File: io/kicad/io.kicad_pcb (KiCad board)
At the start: 2 copper layers, 90 x 88.4 mm, 52 parts, among them J1 Conn_01x04_Pin, J2 Conn_01x04_Pin, J3 pcie_98, U1 B0505MT-1WR4, U2 ESD5344D-TP, U3 ESD5344D-TP, U4 ADUM1201ARZ-RL7, U5 ADUM1201ARZ-RL7, U6 XC6206P332MR, U7 XC6206P332MR, U8 ESD5344D-TP

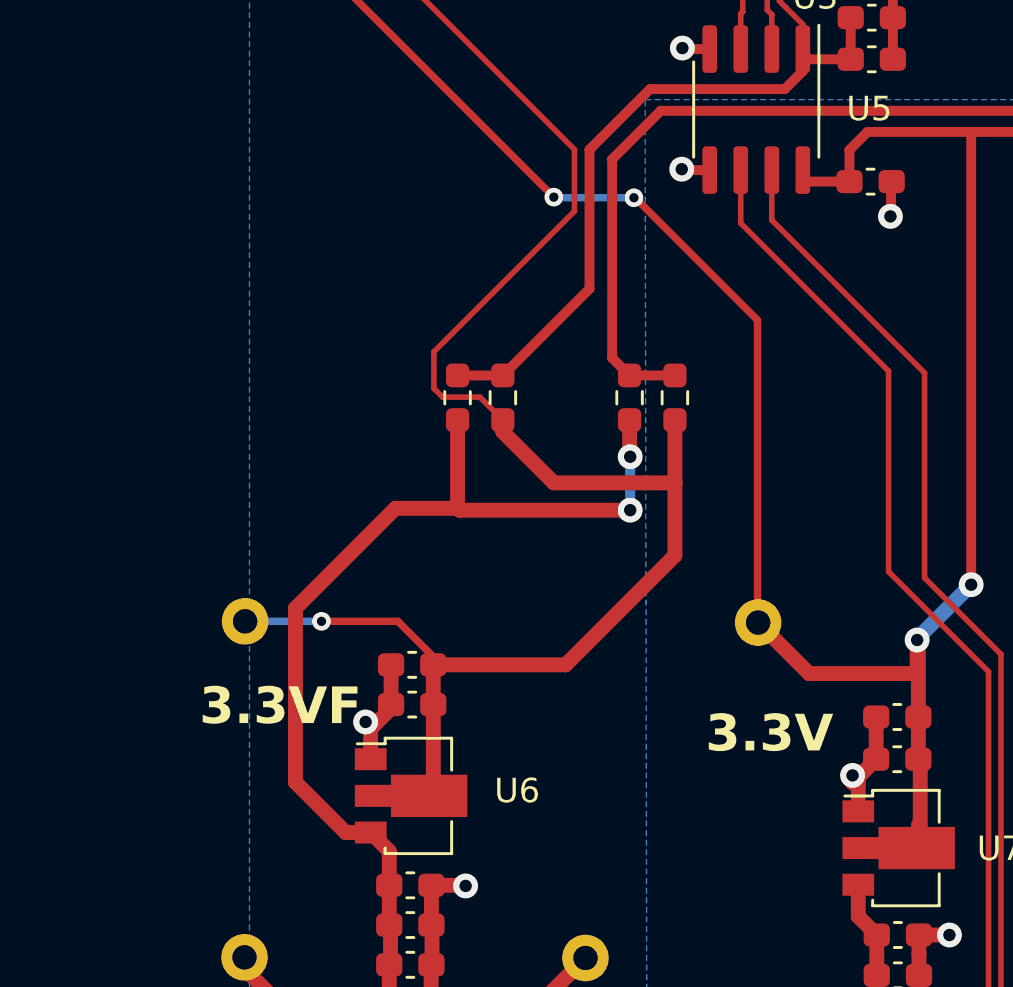
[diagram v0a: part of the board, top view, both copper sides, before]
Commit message: Tweaked the IO card layout
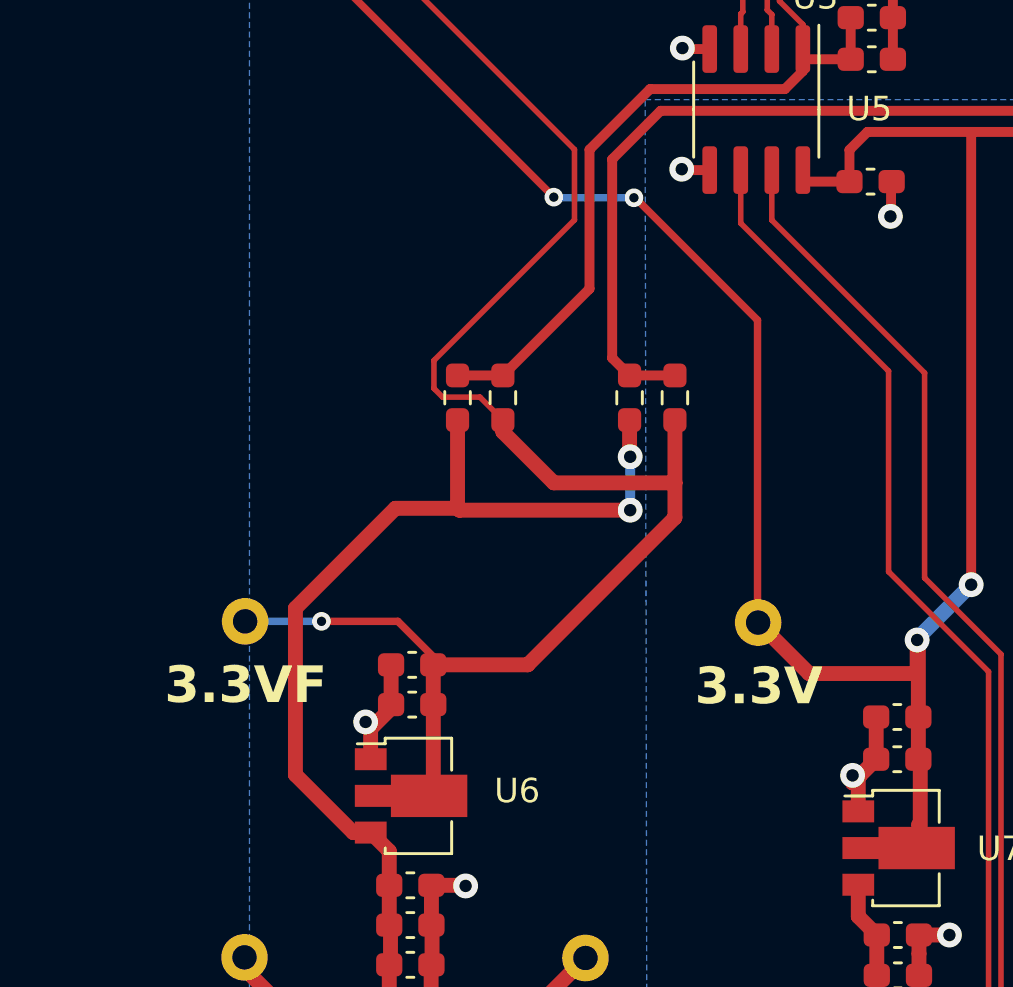
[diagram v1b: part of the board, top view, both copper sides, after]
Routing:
- net /+3V3F: track 71.6 -> 70.7 mm
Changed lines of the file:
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@@
     (effects (font (size 1.5 1.5) (thickness 0.3) bold) (justify bottom mirror))
   )
-  (gr_text "3.3V" (at 8.001 -38.227) (layer "B.SilkS")
-    (effects (font (size 1.5 1.5) (thickness 0.3) bold) (justify left bottom mirror))
+  (gr_text "3.3V" (at 5.2578 -40.259) (layer "B.SilkS")
+    (effects (font (size 1.5 1.5) (thickness 0.3) bold) (justify bottom mirror))
   )
-  (gr_text "3.3VF" (at -14.3002 -39.37) (layer "B.SilkS")
+  (gr_text "3.3VF" (at -15.7226 -40.2336) (layer "B.SilkS")
     (effects (font (size 1.5 1.5) (thickness 0.3) bold) (justify bottom mirror))
   )
@@
     (effects (font (size 1.5 1.5) (thickness 0.3) bold) (justify bottom))
   )
-  (gr_text "3.3V" (at 3.0988 -38.3032) (layer "F.SilkS")
-    (effects (font (size 1.5 1.5) (thickness 0.3) bold) (justify left bottom))
+  (gr_text "3.3V" (at 5.2832 -40.2336) (layer "F.SilkS")
+    (effects (font (size 1.5 1.5) (thickness 0.3) bold) (justify bottom))
   )
   (gr_text "3.3V" (at -18.9484 -83.2104) (layer "F.SilkS")
@@
     (effects (font (size 1.5 1.5) (thickness 0.3) bold) (justify left bottom))
   )
-  (gr_text "3.3VF" (at -14.2748 -39.4208) (layer "F.SilkS")
+  (gr_text "3.3VF" (at -15.6972 -40.2844) (layer "F.SilkS")
     (effects (font (size 1.5 1.5) (thickness 0.3) bold) (justify bottom))
   )
@@
   (via (at -11.8364 -86.614) (size 0.762) (drill 0.381) (layers "F.Cu" "B.Cu") (net 2))
   (via (at 26.9494 -71.7296) (size 0.508) (drill 0.254) (layers "F.Cu" "B.Cu") (net 2))
+  (segment (start -13.6652 -44.2976) (end -9.5758 -48.387) (width 0.6096) (layer "F.Cu") (net 3))
   (segment (start -7.0358 -48.387) (end -6.9596 -48.3108) (width 0.6096) (layer "F.Cu") (net 3))
-  (segment (start -11.6064 -35.1268) (end -13.6652 -37.1856) (width 0.6096) (layer "F.Cu") (net 3))
   (segment (start -7.0358 -51.9957) (end -7.0358 -48.387) (width 0.6096) (layer "F.Cu") (net 3))
   (segment (start -9.8287 -28.4745) (end -9.8287 -29.718) (width 0.6096) (layer "F.Cu") (net 3))
-  (segment (start -10.586 -35.1268) (end -11.6064 -35.1268) (width 0.6096) (layer "F.Cu") (net 3))
+  (segment (start -10.586 -35.1268) (end -11.3016 -35.1268) (width 0.6096) (layer "F.Cu") (net 3))
   (segment (start 0.0254 -50.5714) (end 0.0254 -50.4952) (width 0.6096) (layer "F.Cu") (net 3))
   (segment (start -9.8287 -31.3436) (end -9.8287 -32.9692) (width 0.6096) (layer "F.Cu") (net 3))
@@
   (segment (start -6.9596 -48.3108) (end 0.0254 -48.3108) (width 0.6096) (layer "F.Cu") (net 3))
   (segment (start -11.567 -27.2542) (end -11.049 -27.2542) (width 0.6096) (layer "F.Cu") (net 3))
+  (segment (start -11.3016 -35.1268) (end -13.6652 -37.4904) (width 0.6096) (layer "F.Cu") (net 3))
   (segment (start -15.748 -29.5538) (end -15.748 -30.0228) (width 0.6096) (layer "F.Cu") (net 3))
-  (segment (start -13.6652 -37.1856) (end -13.6652 -44.2976) (width 0.6096) (layer "F.Cu") (net 3))
+  (segment (start -13.6652 -37.4904) (end -13.6652 -44.2976) (width 0.6096) (layer "F.Cu") (net 3))
   (segment (start -9.8287 -34.3695) (end -10.586 -35.1268) (width 0.6096) (layer "F.Cu") (net 3))
   (segment (start -11.567 -27.2542) (end -13.4484 -27.2542) (width 0.6096) (layer "F.Cu") (net 3))
-  (segment (start -13.6652 -44.2976) (end -9.5758 -48.387) (width 0.6096) (layer "F.Cu") (net 3))
+  (segment (start -9.5758 -48.387) (end -7.0358 -48.387) (width 0.6096) (layer "F.Cu") (net 3))
   (segment (start 0.1016 -50.4952) (end 0.0254 -50.5714) (width 0.6096) (layer "F.Cu") (net 3))
   (segment (start 0.0254 -50.4952) (end 0.1016 -50.4952) (width 0.6096) (layer "F.Cu") (net 3))
-  (segment (start -9.5758 -48.387) (end -7.0358 -48.387) (width 0.6096) (layer "F.Cu") (net 3))
   (via (at 0.0254 -50.4952) (size 1.016) (drill 0.508) (layers "F.Cu" "B.Cu") (net 3))
   (via (at 0.0254 -48.3108) (size 1.016) (drill 0.508) (layers "F.Cu" "B.Cu") (net 3))
   (segment (start 0.0254 -50.4952) (end 0.0254 -48.3108) (width 0.4064) (layer "B.Cu") (net 3))
   (segment (start 1.8542 -51.9957) (end 1.8542 -49.4538) (width 0.6096) (layer "F.Cu") (net 4))
-  (segment (start -8.001 -54.7878) (end -2.25301 -60.53579) (width 0.2286) (layer "F.Cu") (net 4))
-  (segment (start 1.8542 -49.403) (end 1.8288 -49.4284) (width 0.6096) (layer "F.Cu") (net 4))
+  (segment (start -5.1816 -51.9957) (end -6.1195 -52.9336) (width 0.2286) (layer "F.Cu") (net 4))
+  (segment (start 1.8542 -48.006) (end 1.8542 -49.403) (width 0.6096) (layer "F.Cu") (net 4))
   (segment (start -9.4742 -43.7642) (end -12.5984 -43.7642) (width 0.3048) (layer "F.Cu") (net 4))
-  (segment (start -5.1816 -51.9957) (end -6.1195 -52.9336) (width 0.2286) (layer "F.Cu") (net 4))
+  (segment (start -8.001 -53.2892) (end -8.001 -54.4322) (width 0.2286) (layer "F.Cu") (net 4))
+  (segment (start -7.6454 -52.9336) (end -8.001 -53.2892) (width 0.2286) (layer "F.Cu") (net 4))
   (segment (start -5.1816 -51.5112) (end -5.1816 -51.9957) (width 0.6096) (layer "F.Cu") (net 4))
   (segment (start 1.8288 -49.4284) (end -3.0988 -49.4284) (width 0.6096) (layer "F.Cu") (net 4))
-  (segment (start -8.001 -53.2892) (end -8.001 -54.7878) (width 0.2286) (layer "F.Cu") (net 4))
+  (segment (start -8.001 -54.4322) (end -2.25301 -60.18019) (width 0.2286) (layer "F.Cu") (net 4))
   (segment (start -8.0286 -42.3186) (end -9.4742 -43.7642) (width 0.3048) (layer "F.Cu") (net 4))
-  (segment (start 1.8542 -46.4566) (end 1.8542 -49.403) (width 0.6096) (layer "F.Cu") (net 4))
-  (segment (start -2.25301 -63.06061) (end -9.3726 -70.1802) (width 0.2286) (layer "F.Cu") (net 4))
-  (segment (start -8.0286 -41.9862) (end -2.6162 -41.9862) (width 0.6096) (layer "F.Cu") (net 4))
   (segment (start -8.0275 -40.2082) (end -8.0264 -40.2071) (width 0.6096) (layer "F.Cu") (net 4))
+  (segment (start -2.25301 -60.18019) (end -2.25301 -63.06061) (width 0.2286) (layer "F.Cu") (net 4))
   (segment (start -9.3726 -70.1802) (end -9.3726 -76.8115) (width 0.2286) (layer "F.Cu") (net 4))
-  (segment (start -7.6454 -52.9336) (end -8.001 -53.2892) (width 0.2286) (layer "F.Cu") (net 4))
+  (segment (start -4.1656 -41.9862) (end 1.8542 -48.006) (width 0.6096) (layer "F.Cu") (net 4))
   (segment (start -6.1195 -52.9336) (end -7.6454 -52.9336) (width 0.2286) (layer "F.Cu") (net 4))
   (segment (start -8.0264 -40.2071) (end -8.0264 -36.72895) (width 0.6096) (layer "F.Cu") (net 4))
+  (segment (start -8.0286 -41.9862) (end -4.1656 -41.9862) (width 0.6096) (layer "F.Cu") (net 4))
   (segment (start -8.0286 -41.8846) (end -8.0286 -40.2093) (width 0.6096) (layer "F.Cu") (net 4))
+  (segment (start -2.25301 -63.06061) (end -9.3726 -70.1802) (width 0.2286) (layer "F.Cu") (net 4))
+  (segment (start 1.8542 -49.403) (end 1.8288 -49.4284) (width 0.6096) (layer "F.Cu") (net 4))
   (segment (start -8.0286 -41.9862) (end -8.0286 -42.3186) (width 0.3048) (layer "F.Cu") (net 4))
-  (segment (start -2.25301 -60.53579) (end -2.25301 -63.06061) (width 0.2286) (layer "F.Cu") (net 4))
   (segment (start -3.0988 -49.4284) (end -5.1816 -51.5112) (width 0.6096) (layer "F.Cu") (net 4))
   (segment (start 1.8542 -49.4538) (end 1.8288 -49.4284) (width 0.6096) (layer "F.Cu") (net 4))
   (segment (start -8.0286 -40.2093) (end -8.0275 -40.2082) (width 0.6096) (layer "F.Cu") (net 4))
-  (segment (start -2.6162 -41.9862) (end 1.8542 -46.4566) (width 0.6096) (layer "F.Cu") (net 4))
   (via (at -12.5984 -43.7642) (size 0.762) (drill 0.381) (layers "F.Cu" "B.Cu") (net 4))
   (segment (start -15.6972 -43.7642) (end -12.5984 -43.7642) (width 0.3048) (layer "B.Cu") (net 4))

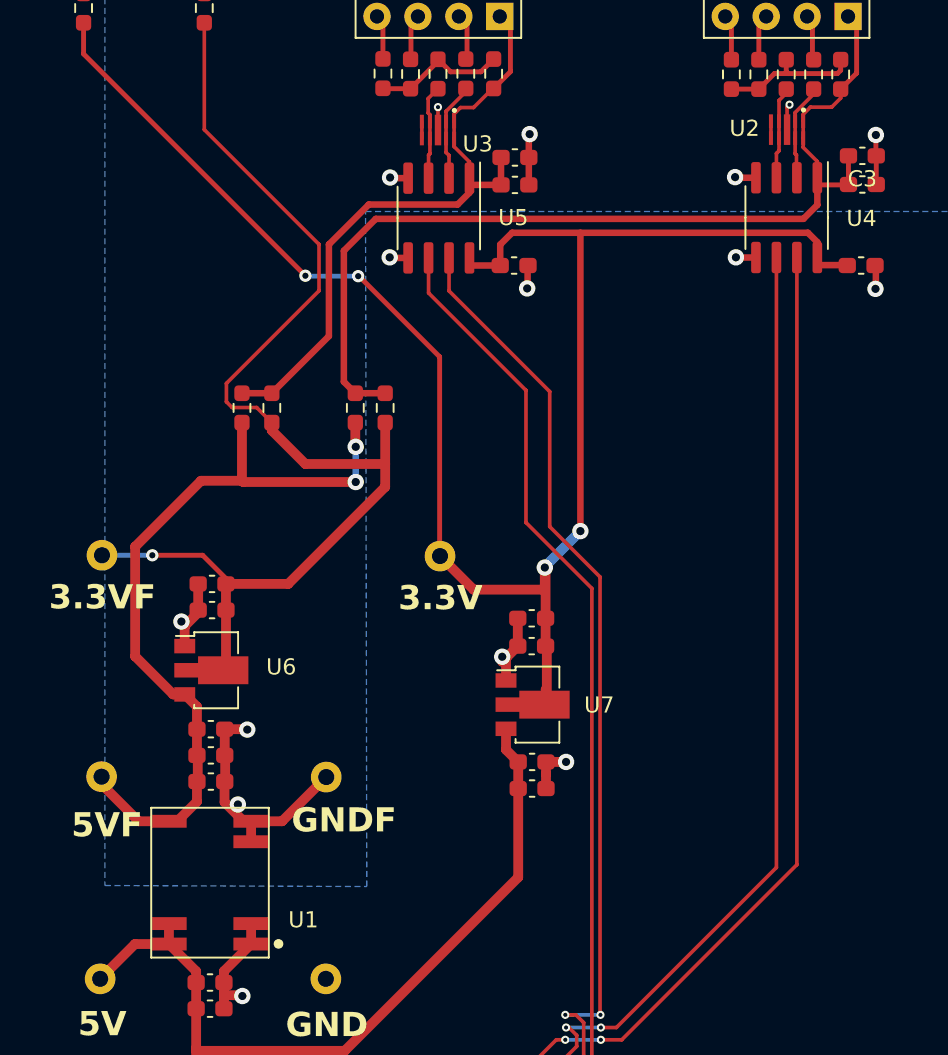
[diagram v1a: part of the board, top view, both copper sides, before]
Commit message: Updated JLCPCB part positioning.
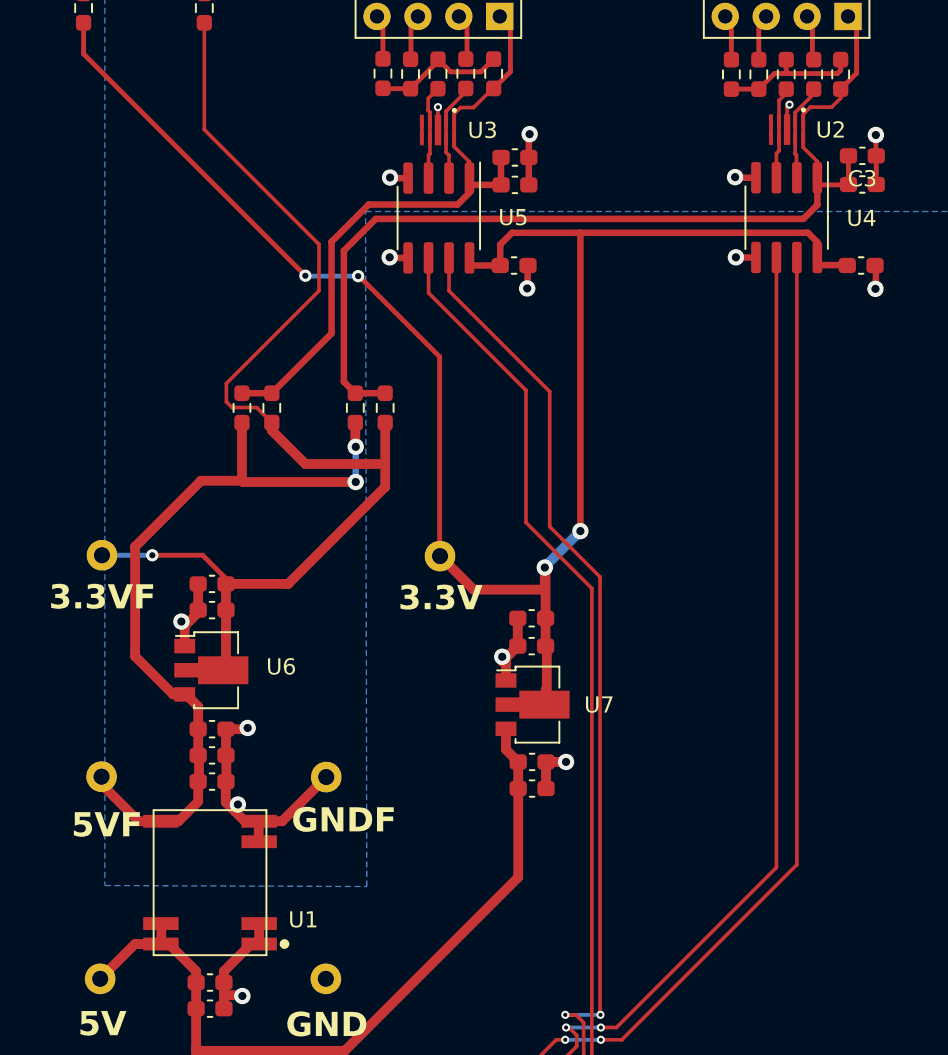
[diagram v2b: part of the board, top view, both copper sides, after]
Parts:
- moved C17 0.08 mm to (-8.89, -33.0)
- moved C5 0.08 mm to (-8.89, -29.7)
- moved C8 0.08 mm to (-8.89, -31.3)

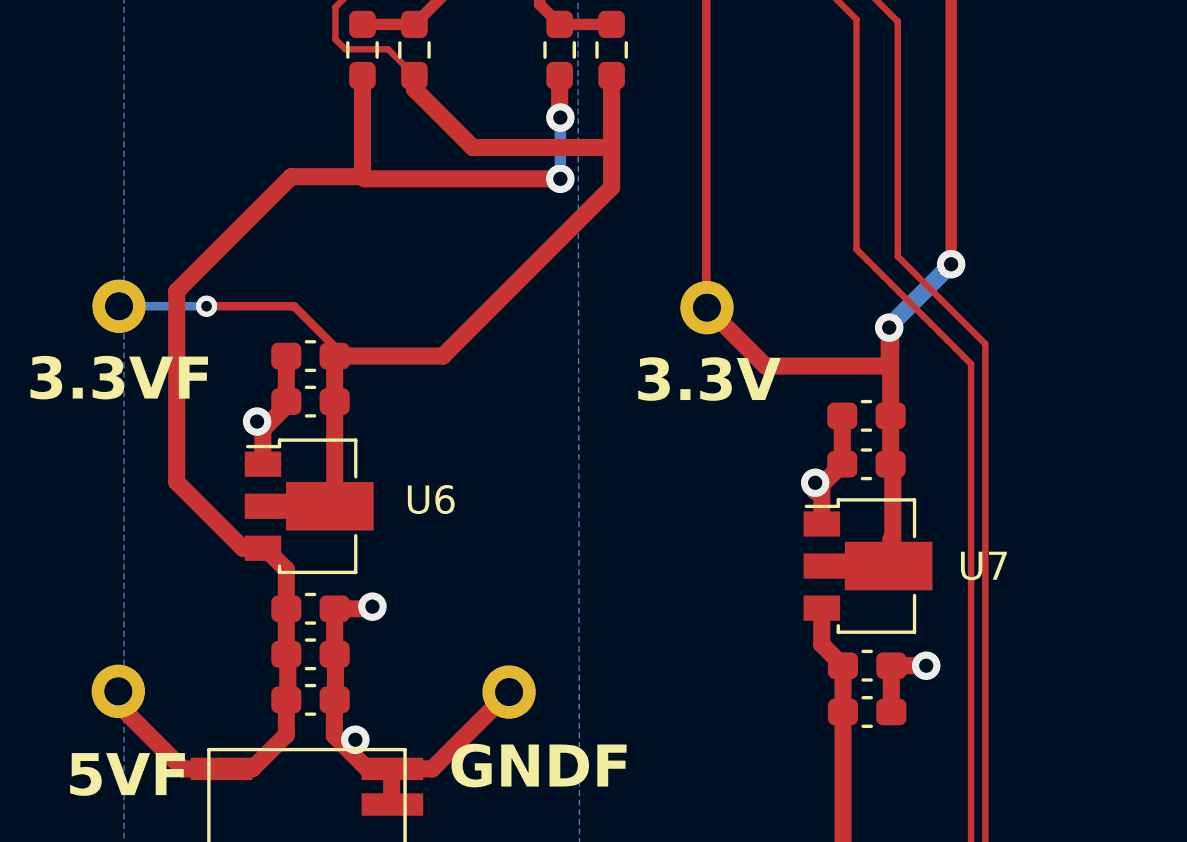
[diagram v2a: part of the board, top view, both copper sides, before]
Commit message: Fixed the part numbers and footpring of the IO board's 3.3V regulators.
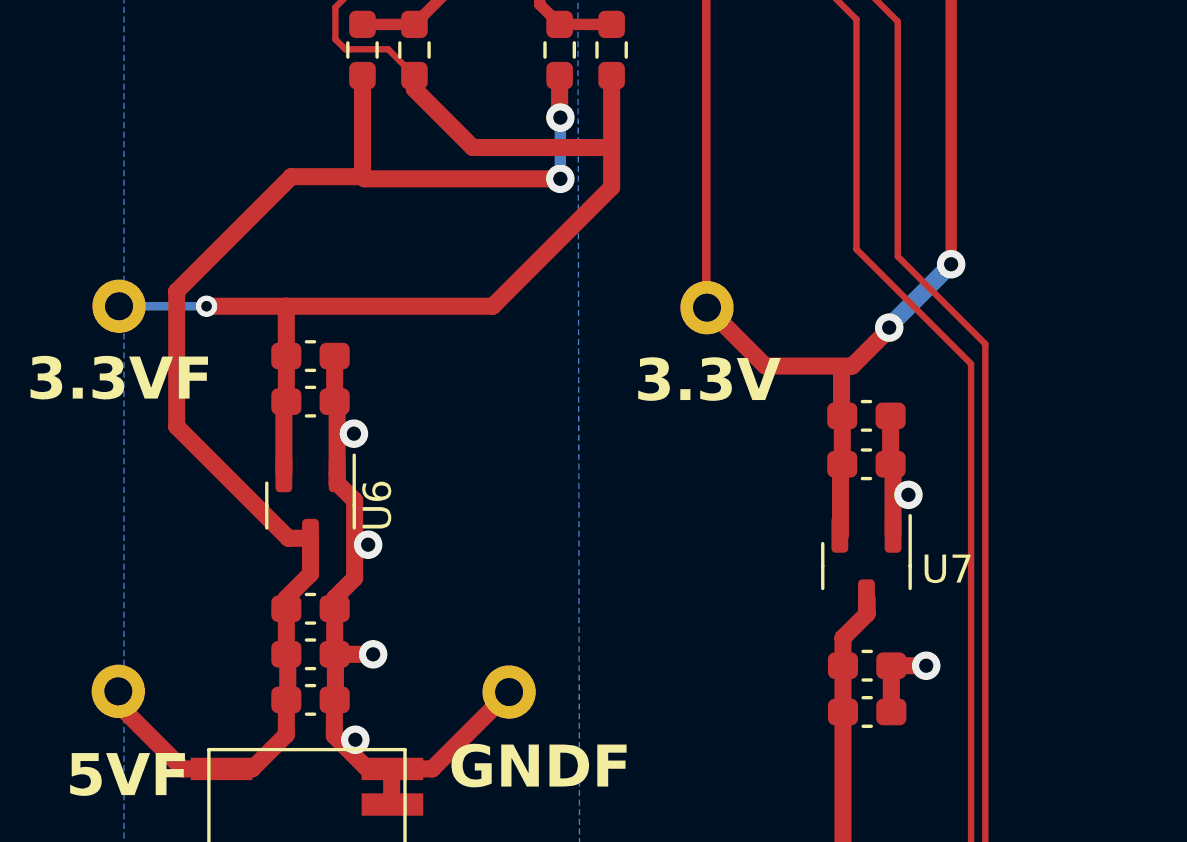
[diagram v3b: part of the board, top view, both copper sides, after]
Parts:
- U6, U7: footprint Package_TO_SOT_SMD:SOT-89-3 -> Package_TO_SOT_SMD:SOT-23-3
- moved U7 0.36 mm to (10.9, -34.5), turned to -90 degrees
- moved U6 0.26 mm to (-8.89, -36.7), turned to -90 degrees
- turned C12 to 180 degrees
- turned C15 to 180 degrees
- turned C16 to 180 degrees
- turned C9 to 180 degrees
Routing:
- net GND1: track 39.1 -> 44.5 mm, vias 10 -> 11
- net +3.3V: track 108.8 -> 105.5 mm
- net GND: track 58.2 -> 57.2 mm
- net /+5VF: track 48.6 -> 49.5 mm
- net /+3V3F: track 70.7 -> 69.9 mm
